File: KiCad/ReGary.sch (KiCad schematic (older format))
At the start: 10 parts, among them U4 SN74CBT16210, U5 SN74CBT16210, U6 SN74CBT16210, U7 SN74CBT16210, U8 PLCC_84_plug, U9 PLCC_84_plug

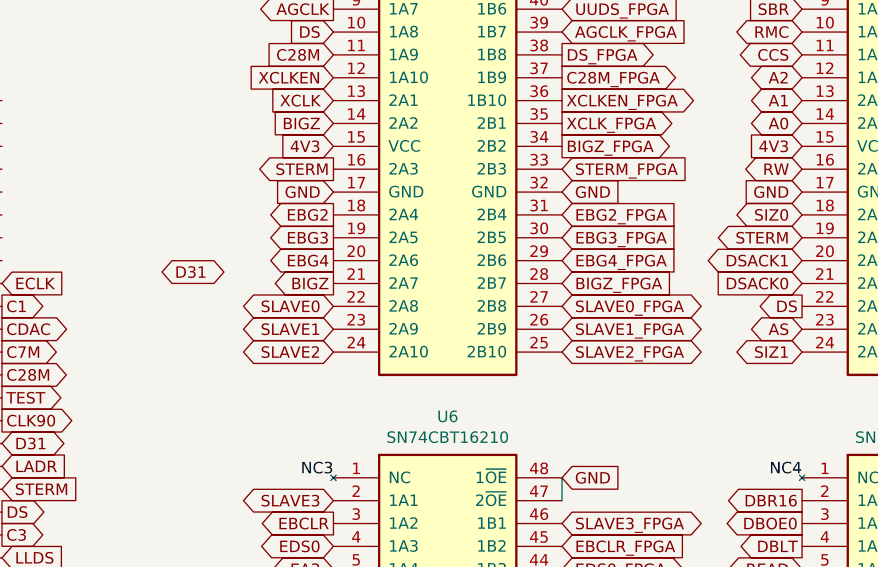
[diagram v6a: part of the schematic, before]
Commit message: More FPGA pin assignments and routing
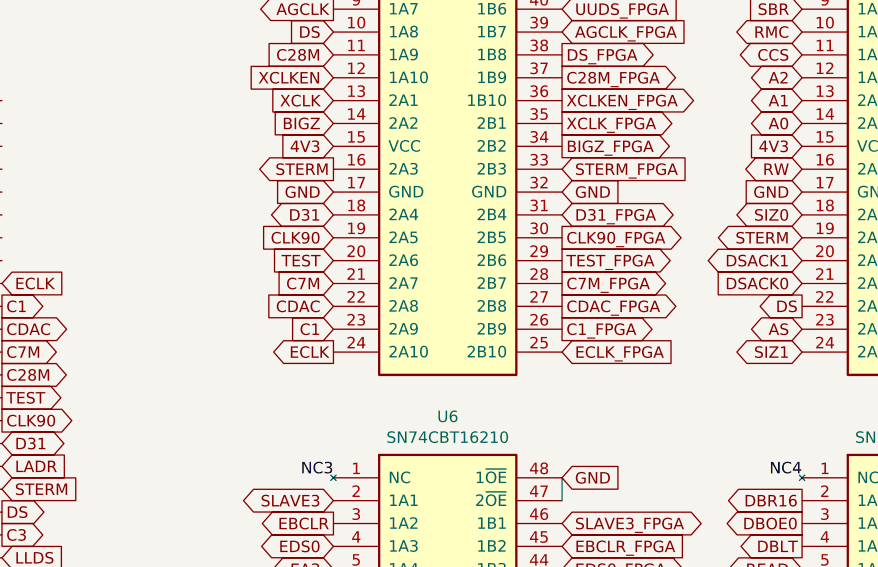
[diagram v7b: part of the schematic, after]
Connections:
- net EBG2 is gone; now on net D31: U4.18 (2A4)
- net EBG3 is gone; now on net CLK90: U4.19 (2A5)
- net EBG3_FPGA is gone; now on net CLK90_FPGA: U4.30 (2B5)
- net EBG4 is gone; now on net TEST: U4.20 (2A6)
- net SLAVE0 is gone; now on net CDAC: U4.22 (2A8)
- net SLAVE0_FPGA is gone; now on net CDAC_FPGA: U4.27 (2B8)
- net SLAVE1 is gone; now on net C1: U4.23 (2A9)
- net SLAVE2 is gone; now on net ECLK: U4.24 (2A10)
- net BIGZ: no longer U4.21 (2A7)
- net BIGZ_FPGA: no longer U4.28 (2B7)
- net C7M: now also U4.21 (2A7)
- net C7M_FPGA: now also U4.28 (2B7)
- net EBG2_FPGA renamed D31_FPGA
- net EBG4_FPGA renamed TEST_FPGA
- net SLAVE1_FPGA renamed C1_FPGA
- net SLAVE2_FPGA renamed ECLK_FPGA
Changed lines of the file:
@@
 Text GLabel 8150 1950 2    50   Output ~ 0
 DS_FPGA
-Text GLabel 8150 2650 2    50   Input ~ 0
-EBG2_FPGA
-Text GLabel 8150 2750 2    50   Input ~ 0
-EBG3_FPGA
-Text GLabel 8150 2850 2    50   Input ~ 0
-EBG4_FPGA
-Text GLabel 8150 2950 2    50   Input ~ 0
-BIGZ_FPGA
-Text GLabel 8150 3050 2    50   BiDi ~ 0
-SLAVE0_FPGA
-Text GLabel 8150 3150 2    50   BiDi ~ 0
-SLAVE1_FPGA
-Text GLabel 8150 3250 2    50   BiDi ~ 0
-SLAVE2_FPGA
 Text GLabel 10200 1150 2    50   Output ~ 0
 WAIT_FPGA
@@
 Text GLabel 7150 4200 0    50   BiDi ~ 0
 EA3
-Text GLabel 7150 2650 0    50   Output ~ 0
-EBG2
-Text GLabel 7150 2750 0    50   Output ~ 0
-EBG3
-Text GLabel 7150 2850 0    50   Output ~ 0
-EBG4
-Text GLabel 7150 2950 0    50   Output ~ 0
-BIGZ
-Text GLabel 7150 3050 0    50   BiDi ~ 0
-SLAVE0
-Text GLabel 7150 3150 0    50   BiDi ~ 0
-SLAVE1
-Text GLabel 7150 3250 0    50   BiDi ~ 0
-SLAVE2
 Text GLabel 7150 3900 0    50   BiDi ~ 0
 SLAVE3
@@
 Text GLabel 8150 2450 2    50   Input ~ 0
 STERM_FPGA
-Text GLabel 6400 2900 2    50   BiDi ~ 0
+Text GLabel 7150 2650 0    50   BiDi ~ 0
 D31
 Text GLabel 8150 2350 2    50   Output ~ 0
@@
 Text GLabel 8150 2050 2    50   Output ~ 0
 C28M_FPGA
+Text GLabel 8150 2650 2    50   BiDi ~ 0
+D31_FPGA
+Text GLabel 7150 2750 0    50   Input ~ 0
+CLK90
+Text GLabel 8150 2750 2    50   Output ~ 0
+CLK90_FPGA
+Text GLabel 8150 2850 2    50   Output ~ 0
+TEST_FPGA
+Text GLabel 7150 2850 0    50   Input ~ 0
+TEST
+Text GLabel 7150 2950 0    50   Input ~ 0
+C7M
+Text GLabel 8150 2950 2    50   Output ~ 0
+C7M_FPGA
+Text GLabel 7150 3050 0    50   Input ~ 0
+CDAC
+Text GLabel 8150 3050 2    50   Output ~ 0
+CDAC_FPGA
+Text GLabel 7150 3150 0    50   Input ~ 0
+C1
+Text GLabel 8150 3150 2    50   Output ~ 0
+C1_FPGA
+Text GLabel 7150 3250 0    50   Output ~ 0
+ECLK
+Text GLabel 8150 3250 2    50   Input ~ 0
+ECLK_FPGA
 $EndSCHEMATC

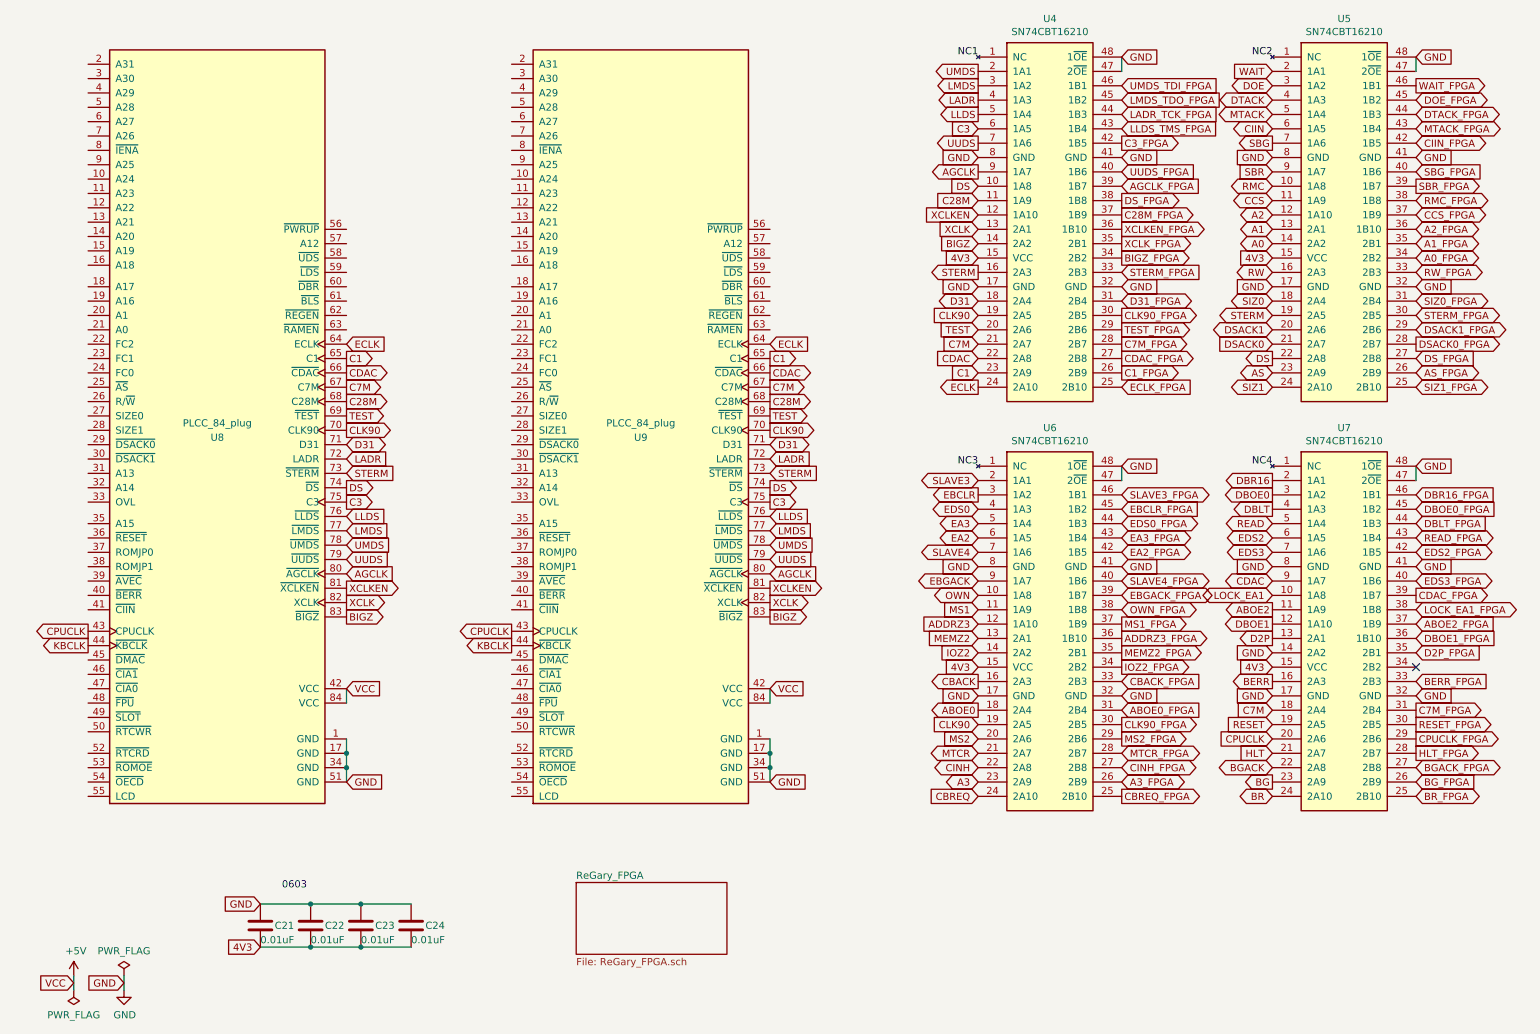
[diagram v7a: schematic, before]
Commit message: More signal to pin assignments and routing
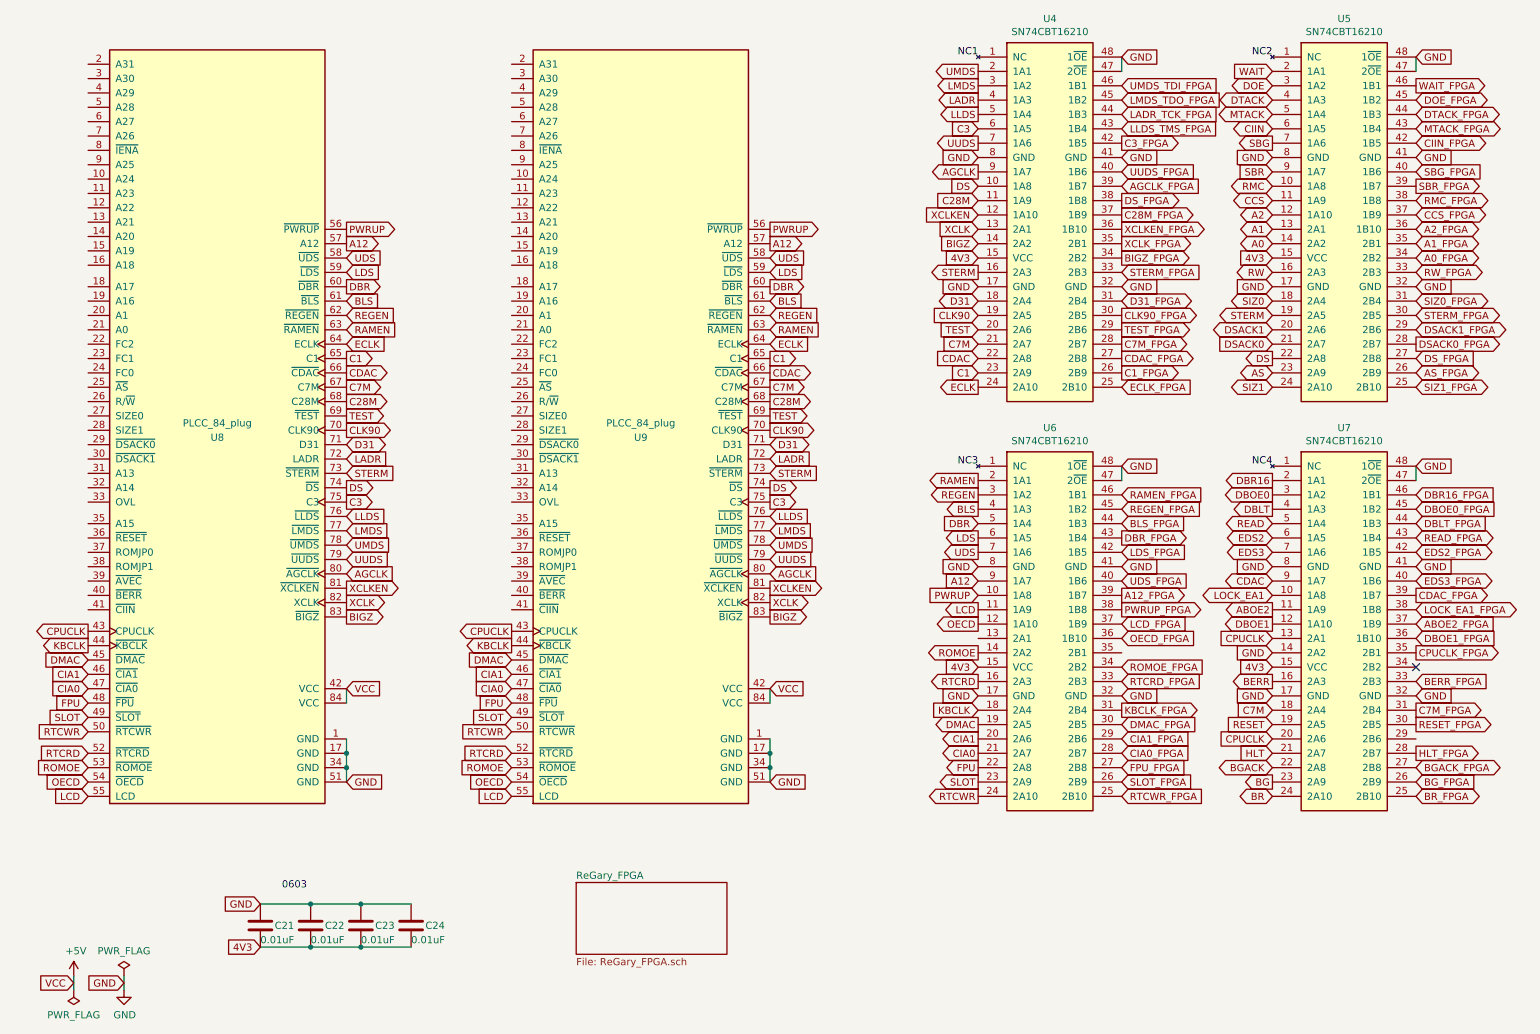
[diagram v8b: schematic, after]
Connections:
- net A3 is gone; now on net SLOT: U6.23 (2A9)
- net ABOE0 is gone; now on net KBCLK: U6.18 (2A4)
- net ADDRZ3 is gone; now on net OECD: U6.12 (1A10)
- net CBACK is gone; now on net RTCRD: U6.16 (2A3)
- net CBREQ is gone; now on net RTCWR: U6.24 (2A10)
- net CINH is gone; now on net FPU: U6.22 (2A8)
- net D2P is gone; now on net CPUCLK: U7.13 (2A1)
- net D2P_FPGA is gone; now on net CPUCLK_FPGA: U7.35 (2B1)
- net EA2 is gone; now on net LDS: U6.6 (1A5)
- net EA3 is gone; now on net DBR: U6.5 (1A4)
- net EBCLR is gone; now on net REGEN: U6.3 (1A2)
- net EBGACK is gone; now on net A12: U6.9 (1A7)
- net EDS0 is gone; now on net BLS: U6.4 (1A3)
- net IOZ2 is gone; now on net ROMOE: U6.14 (2A2)
- net MS1 is gone; now on net LCD: U6.11 (1A9)
- net MS2 is gone; now on net CIA1: U6.20 (2A6)
- net MTCR is gone; now on net CIA0: U6.21 (2A7)
- net OWN is gone; now on net PWRUP: U6.10 (1A8)
- net SLAVE3 is gone; now on net RAMEN: U6.2 (1A1)
- net SLAVE4 is gone; now on net UDS: U6.7 (1A6)
- net CLK90: no longer U6.19 (2A5)
- net CLK90_FPGA: no longer U6.30 (2B5)
- net CPUCLK_FPGA: no longer U7.29 (2B6)
- net DMAC: now reaches U9.45 (~DMAC)
- net DMAC: now also U6.19 (2A5), U8.45 (~DMAC)
- net CIA1: now reaches U9.46 (~CIA1)
- net CIA1: now also U8.46 (~CIA1)
- net CIA0: now reaches U9.47 (~CIA0)
- net CIA0: now also U8.47 (~CIA0)
- net FPU: now reaches U9.48 (~FPU)
- net FPU: now also U8.48 (~FPU)
- net SLOT: now reaches U9.49 (~SLOT)
- net SLOT: now also U8.49 (~SLOT)
- net RTCWR: now reaches U9.50 (~RTCWR)
- net RTCWR: now also U8.50 (~RTCWR)
- net RTCRD: now reaches U9.52 (~RTCRD)
- net RTCRD: now also U8.52 (~RTCRD)
- net ROMOE: now reaches U9.53 (~ROMOE)
- net ROMOE: now also U8.53 (~ROMOE)
- net OECD: now reaches U9.54 (~OECD)
- net OECD: now also U8.54 (~OECD)
- net LCD: now reaches U9.55 (LCD)
- net LCD: now also U8.55 (LCD)
- net PWRUP: now reaches U9.56 (~PWRUP)
- net PWRUP: now also U8.56 (~PWRUP)
- net A12: now reaches U9.57 (A12)
- net A12: now also U8.57 (A12)
- net UDS: now reaches U9.58 (~UDS)
- net UDS: now also U8.58 (~UDS)
- net LDS: now reaches U9.59 (~LDS)
- net LDS: now also U8.59 (~LDS)
- net DBR: now reaches U9.60 (~DBR)
- net DBR: now also U8.60 (~DBR)
- net BLS: now reaches U9.61 (~BLS)
- net BLS: now also U8.61 (~BLS)
- net REGEN: now reaches U9.62 (~REGEN)
- net REGEN: now also U8.62 (~REGEN)
- net RAMEN: now reaches U9.63 (~RAMEN)
- net RAMEN: now also U8.63 (~RAMEN)
- net A3_FPGA renamed SLOT_FPGA
- net ABOE0_FPGA renamed KBCLK_FPGA
- net ADDRZ3_FPGA renamed OECD_FPGA
- net CBACK_FPGA renamed RTCRD_FPGA
- net CBREQ_FPGA renamed RTCWR_FPGA
- net CINH_FPGA renamed FPU_FPGA
- net EA2_FPGA renamed LDS_FPGA
- net EA3_FPGA renamed DBR_FPGA
- net EBCLR_FPGA renamed REGEN_FPGA
- net EBGACK_FPGA renamed A12_FPGA
- net EDS0_FPGA renamed BLS_FPGA
- net IOZ2_FPGA renamed ROMOE_FPGA
- net MEMZ2: no longer names the net of U6.13 (2A1)
- net MEMZ2_FPGA: no longer names the net of U6.35 (2B1)
- net MS1_FPGA renamed LCD_FPGA
- net MS2_FPGA renamed CIA1_FPGA
- net MTCR_FPGA renamed CIA0_FPGA
- net OWN_FPGA renamed PWRUP_FPGA
- net SLAVE3_FPGA renamed RAMEN_FPGA
- net SLAVE4_FPGA renamed UDS_FPGA
- new net DMAC_FPGA: U6.30 (2B5)
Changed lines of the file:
@@
 Text GLabel 10200 3150 2    50   BiDi ~ 0
 AS_FPGA
-Text GLabel 8150 4000 2    50   BiDi ~ 0
-SLAVE3_FPGA
+Text GLabel 8150 4000 2    50   Input ~ 0
+RAMEN_FPGA
 Text GLabel 8150 4100 2    50   Input ~ 0
-EBCLR_FPGA
-Text GLabel 8150 4200 2    50   BiDi ~ 0
-EDS0_FPGA
-Text GLabel 8150 4300 2    50   BiDi ~ 0
-EA3_FPGA
-Text GLabel 8150 4400 2    50   BiDi ~ 0
-EA2_FPGA
-Text GLabel 8150 4700 2    50   BiDi ~ 0
-EBGACK_FPGA
-Text GLabel 8150 4800 2    50   BiDi ~ 0
-OWN_FPGA
-Text GLabel 8150 4900 2    50   Output ~ 0
-MS1_FPGA
-Text GLabel 8150 5000 2    50   Output ~ 0
-ADDRZ3_FPGA
-Text GLabel 8150 5100 2    50   Output ~ 0
-MEMZ2_FPGA
-Text GLabel 8150 5200 2    50   Output ~ 0
-IOZ2_FPGA
-Text GLabel 8150 5300 2    50   Input ~ 0
-CBACK_FPGA
-Text GLabel 8150 5600 2    50   Output ~ 0
-CLK90_FPGA
-Text GLabel 8150 5500 2    50   Input ~ 0
-ABOE0_FPGA
-Text GLabel 8150 5700 2    50   Output ~ 0
-MS2_FPGA
-Text GLabel 8150 5800 2    50   BiDi ~ 0
-MTCR_FPGA
-Text GLabel 8150 5900 2    50   BiDi ~ 0
-CINH_FPGA
-Text GLabel 8150 6000 2    50   BiDi ~ 0
-A3_FPGA
-Text GLabel 8150 6100 2    50   Output ~ 0
-CBREQ_FPGA
+REGEN_FPGA
+Text GLabel 8150 4200 2    50   Input ~ 0
+BLS_FPGA
+Text GLabel 8150 4300 2    50   Output ~ 0
+DBR_FPGA
 Text GLabel 10200 4000 2    50   Input ~ 0
 DBR16_FPGA
@@
 Text GLabel 10200 5000 2    50   Input ~ 0
 DBOE1_FPGA
-Text GLabel 10200 5100 2    50   Input ~ 0
-D2P_FPGA
 Text GLabel 10200 5300 2    50   Input ~ 0
 BERR_FPGA
@@
 Text GLabel 10200 5800 2    50   Output ~ 0
 HLT_FPGA
-Text GLabel 10200 5700 2    50   Output ~ 0
+Text GLabel 10200 5100 2    50   Output ~ 0
 CPUCLK_FPGA
 Text GLabel 10200 5900 2    50   BiDi ~ 0
@@
 Text GLabel 8150 2250 2    50   Output ~ 0
 XCLK_FPGA
-Text GLabel 8150 4600 2    50   BiDi ~ 0
-SLAVE4_FPGA
 Text GLabel 9200 1950 0    50   BiDi ~ 0
 CCS
@@
 Text GLabel 9200 4600 0    50   BiDi ~ 0
 CDAC
-Text GLabel 9200 5000 0    50   Output ~ 0
-D2P
 Text GLabel 9200 4900 0    50   Output ~ 0
 DBOE1
@@
 Text GLabel 9200 4800 0    50   Output ~ 0
 ABOE2
-Text GLabel 7150 5500 0    50   Output ~ 0
-ABOE0
-Text GLabel 7150 5700 0    50   Input ~ 0
-MS2
-Text GLabel 7150 5800 0    50   BiDi ~ 0
-MTCR
-Text GLabel 7150 5900 0    50   BiDi ~ 0
-CINH
-Text GLabel 7150 6000 0    50   BiDi ~ 0
-A3
-Text GLabel 7150 6100 0    50   Input ~ 0
-CBREQ
-Text GLabel 7150 5300 0    50   Output ~ 0
-CBACK
-Text GLabel 7150 5100 0    50   Input ~ 0
-IOZ2
-Text GLabel 7150 5000 0    50   Input ~ 0
-MEMZ2
-Text GLabel 7150 4900 0    50   Input ~ 0
-ADDRZ3
-Text GLabel 7150 4800 0    50   Input ~ 0
-MS1
-Text GLabel 7150 4700 0    50   BiDi ~ 0
-OWN
-Text GLabel 7150 4600 0    50   BiDi ~ 0
-EBGACK
-Text GLabel 7150 5600 0    50   Input ~ 0
-CLK90
-Text GLabel 7150 4400 0    50   BiDi ~ 0
-SLAVE4
-Text GLabel 7150 4300 0    50   BiDi ~ 0
-EA2
-Text GLabel 7150 4200 0    50   BiDi ~ 0
-EA3
-Text GLabel 7150 3900 0    50   BiDi ~ 0
-SLAVE3
-Text GLabel 7150 4000 0    50   Output ~ 0
-EBCLR
-Text GLabel 7150 4100 0    50   BiDi ~ 0
-EDS0
+Text GLabel 2750 2450 2    50   Input ~ 0
+LDS
+Text GLabel 2750 2550 2    50   Output ~ 0
+DBR
+Text GLabel 5700 2850 2    50   Input ~ 0
+RAMEN
+Text GLabel 5700 2750 2    50   Input ~ 0
+REGEN
+Text GLabel 2750 2650 2    50   Input ~ 0
+BLS
 $Comp
 L ReGary:Fat_Gary_socket U9
@@
 Text GLabel 8150 3250 2    50   Input ~ 0
 ECLK_FPGA
+Text GLabel 7150 3900 0    50   Output ~ 0
+RAMEN
+Text GLabel 7150 4000 0    50   Output ~ 0
+REGEN
+Text GLabel 2750 2850 2    50   Input ~ 0
+RAMEN
+Text GLabel 2750 2750 2    50   Input ~ 0
+REGEN
+Text GLabel 7150 4100 0    50   Output ~ 0
+BLS
+Text GLabel 5700 2650 2    50   Input ~ 0
+BLS
+Text GLabel 5700 2550 2    50   Output ~ 0
+DBR
+Text GLabel 7150 4200 0    50   Input ~ 0
+DBR
+Text GLabel 5700 2450 2    50   Input ~ 0
+LDS
+Text GLabel 9200 5000 0    50   Input ~ 0
+CPUCLK
+Text GLabel 7150 5500 0    50   Input ~ 0
+KBCLK
+Text GLabel 8150 5500 2    50   Output ~ 0
+KBCLK_FPGA
+Text GLabel 7150 5600 0    50   Output ~ 0
+DMAC
+Text GLabel 7150 5700 0    50   Output ~ 0
+CIA1
+Text GLabel 7150 5800 0    50   Output ~ 0
+CIA0
+Text GLabel 7150 5900 0    50   Output ~ 0
+FPU
+Text GLabel 7150 6000 0    50   Output ~ 0
+SLOT
+Text GLabel 7150 6100 0    50   Output ~ 0
+RTCWR
+Text GLabel 950  5650 0    50   Input ~ 0
+RTCWR
+Text GLabel 950  5550 0    50   Input ~ 0
+SLOT
+Text GLabel 950  5450 0    50   Input ~ 0
+FPU
+Text GLabel 950  5350 0    50   Input ~ 0
+CIA0
+Text GLabel 950  5250 0    50   Input ~ 0
+CIA1
+Text GLabel 950  5150 0    50   Input ~ 0
+DMAC
+Text GLabel 3900 5650 0    50   Input ~ 0
+RTCWR
+Text GLabel 3900 5550 0    50   Input ~ 0
+SLOT
+Text GLabel 3900 5450 0    50   Input ~ 0
+FPU
+Text GLabel 3900 5350 0    50   Input ~ 0
+CIA0
+Text GLabel 3900 5250 0    50   Input ~ 0
+CIA1
+Text GLabel 3900 5150 0    50   Input ~ 0
+DMAC
+Text GLabel 8150 5600 2    50   Input ~ 0
+DMAC_FPGA
+Text GLabel 8150 5700 2    50   Input ~ 0
+CIA1_FPGA
+Text GLabel 8150 5800 2    50   Input ~ 0
+CIA0_FPGA
+Text GLabel 8150 5900 2    50   Input ~ 0
+FPU_FPGA
+Text GLabel 8150 6000 2    50   Input ~ 0
+SLOT_FPGA
+Text GLabel 8150 6100 2    50   Input ~ 0
+RTCWR_FPGA
+Text GLabel 950  5800 0    50   Input ~ 0
+RTCRD
+Text GLabel 950  5900 0    50   Input ~ 0
+ROMOE
+Text GLabel 950  6000 0    50   Input ~ 0
+OECD
+Text GLabel 950  6100 0    50   Input ~ 0
+LCD
+Text GLabel 3900 5800 0    50   Input ~ 0
+RTCRD
+Text GLabel 3900 5900 0    50   Input ~ 0
+ROMOE
+Text GLabel 3900 6000 0    50   Input ~ 0
+OECD
+Text GLabel 3900 6100 0    50   Input ~ 0
+LCD
+Text GLabel 8150 5300 2    50   Input ~ 0
+RTCRD_FPGA
+Text GLabel 8150 5200 2    50   Input ~ 0
+ROMOE_FPGA
+Text GLabel 8150 5000 2    50   Input ~ 0
+OECD_FPGA
+Text GLabel 8150 4900 2    50   Input ~ 0
+LCD_FPGA
+Text GLabel 7150 5300 0    50   Output ~ 0
+RTCRD
+Text GLabel 7150 5100 0    50   Output ~ 0
+ROMOE
+Text GLabel 7150 4900 0    50   Output ~ 0
+OECD
+Text GLabel 7150 4800 0    50   Output ~ 0
+LCD
+Text GLabel 2750 2350 2    50   Input ~ 0
+UDS
+Text GLabel 5700 2350 2    50   Input ~ 0
+UDS
+Text GLabel 7150 4300 0    50   Output ~ 0
+LDS
+Text GLabel 7150 4400 0    50   Output ~ 0
+UDS
+Text GLabel 8150 4400 2    50   Input ~ 0
+LDS_FPGA
+Text GLabel 8150 4600 2    50   Input ~ 0
+UDS_FPGA
+Text GLabel 2750 2250 2    50   Output ~ 0
+A12
+Text GLabel 2750 2150 2    50   Output ~ 0
+PWRUP
+Text GLabel 5700 2250 2    50   Output ~ 0
+A12
+Text GLabel 5700 2150 2    50   Output ~ 0
+PWRUP
+Text GLabel 7150 4600 0    50   Input ~ 0
+A12
+Text GLabel 7150 4700 0    50   Input ~ 0
+PWRUP
+Text GLabel 8150 4700 2    50   Output ~ 0
+A12_FPGA
+Text GLabel 8150 4800 2    50   Output ~ 0
+PWRUP_FPGA
 $EndSCHEMATC
